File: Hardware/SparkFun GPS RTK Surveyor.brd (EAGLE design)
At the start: 69.1 x 110.1 mm, 189 parts, among them J16 microSD, J17 Qwiic Right Angle, J3 USB Female Type C Connector, J4 Qwiic Right Angle, J5 USB Female Type C Connector, J6 Start Base, J7 Power Switch, Q2 MBT3904DW1T1, U10 MCP73833, U2 3.3V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

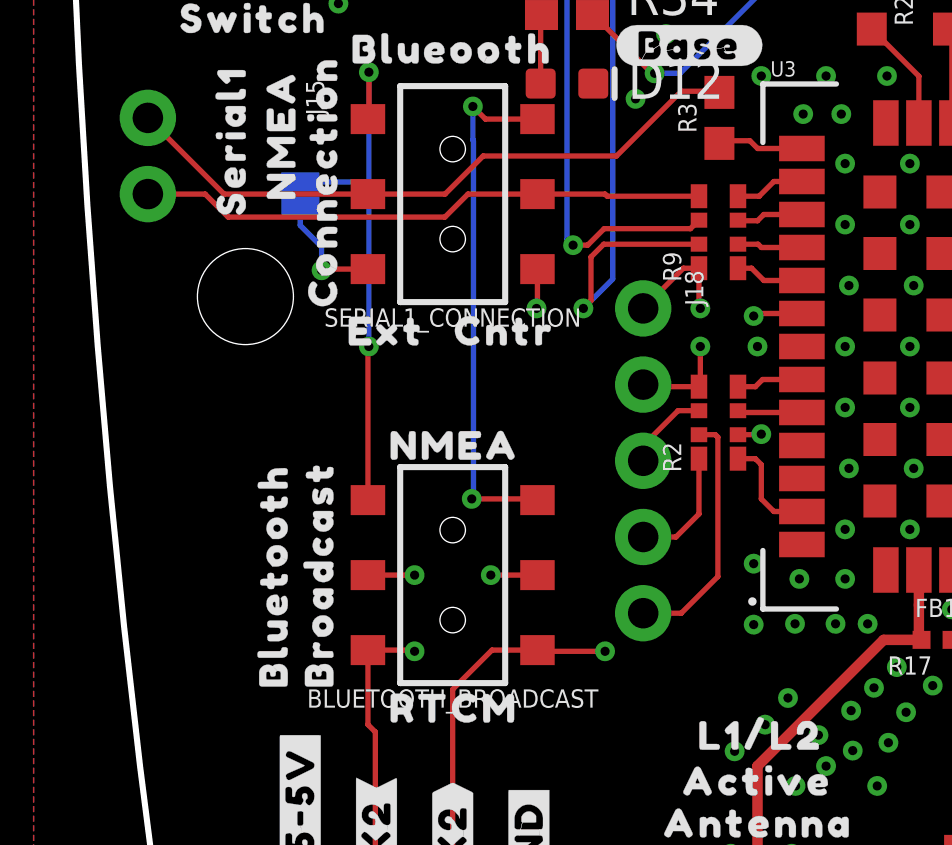
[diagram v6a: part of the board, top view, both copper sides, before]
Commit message: Add slide switch to optionally route PPS to Data port
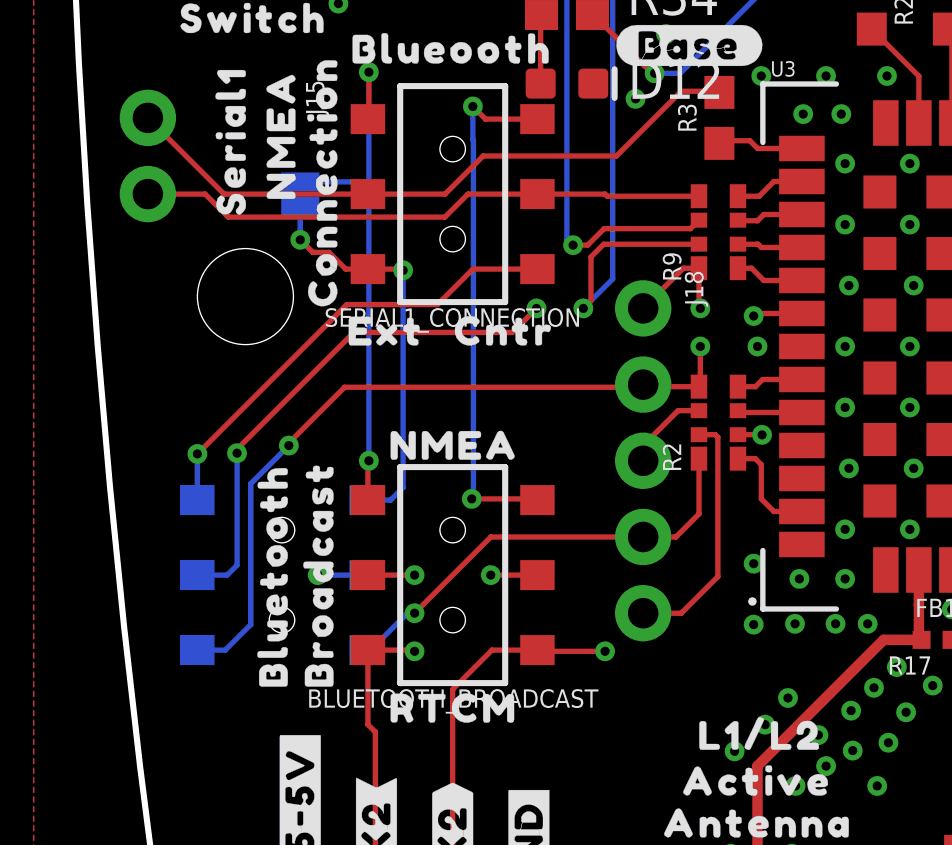
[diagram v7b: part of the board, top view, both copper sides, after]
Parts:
- added U$89: (no value), output:DATA2
- added U$90: (no value), output:PORT3
- added U$91: (no value), output:PPS#RESET0
- added U$92: (no value), output:NMEA#SERIAL1
- added ZED_CONTROL: (no value), SparkFun-Switches:SWITCH_DPDT_SMD_AYZ0202
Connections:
- new net EXTERNAL_SERIAL1_RXI/ZED_!RESET!: J12.2, J2.3, ZED_CONTROL.5
- new net EXTERNAL_SERIAL1_TXO/PPS: J12.3, J2.2, ZED_CONTROL.2
- net ESP_27/ZED_!RESET!: now also ZED_CONTROL.4
- net EXTERNAL_SERIAL1_RXI: now also ZED_CONTROL.6; no longer J12.2, J2.3
- net EXTERNAL_SERIAL1_TXO: now also ZED_CONTROL.3; no longer J12.3, J2.2
- net ZED_PPS_STAT: now also ZED_CONTROL.1
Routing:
- net EXTERNAL_SERIAL1_TXO/PPS: track 0.00 -> 101.6 mm, vias 0 -> 2
- net EXTERNAL_SERIAL1_RXI/ZED_!RESET!: track 0.00 -> 99.7 mm, vias 0 -> 3
- net EXTERNAL_SERIAL1_TXO: track 93.7 -> 13.6 mm
- net EXTERNAL_SERIAL1_RXI: track 83.7 -> 15.4 mm, vias 2 -> 1
- net ESP_27/ZED_!RESET!: track 81.3 -> 102.6 mm, vias 3 -> 4
- net ZED_PPS_STAT: track 55.8 -> 66.6 mm, vias 3 -> 4

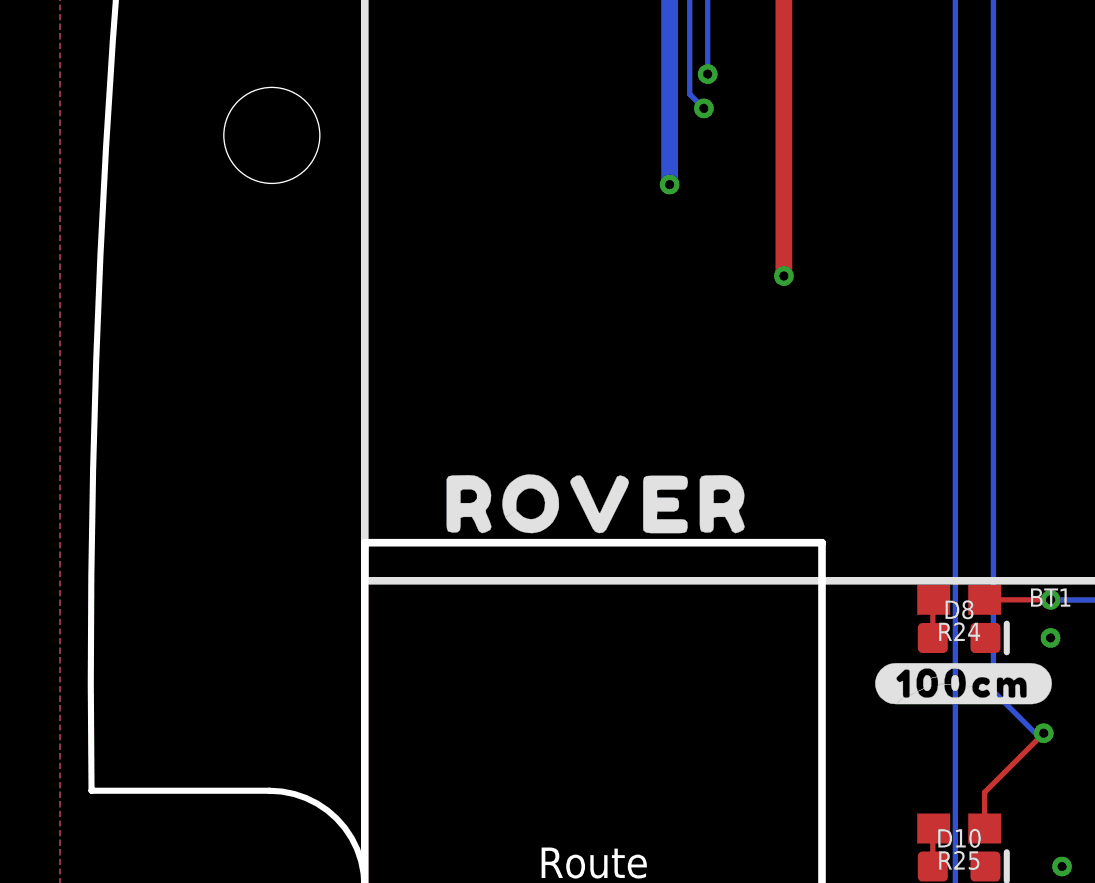
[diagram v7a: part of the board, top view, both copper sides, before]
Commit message: Add internal Qwiic connector
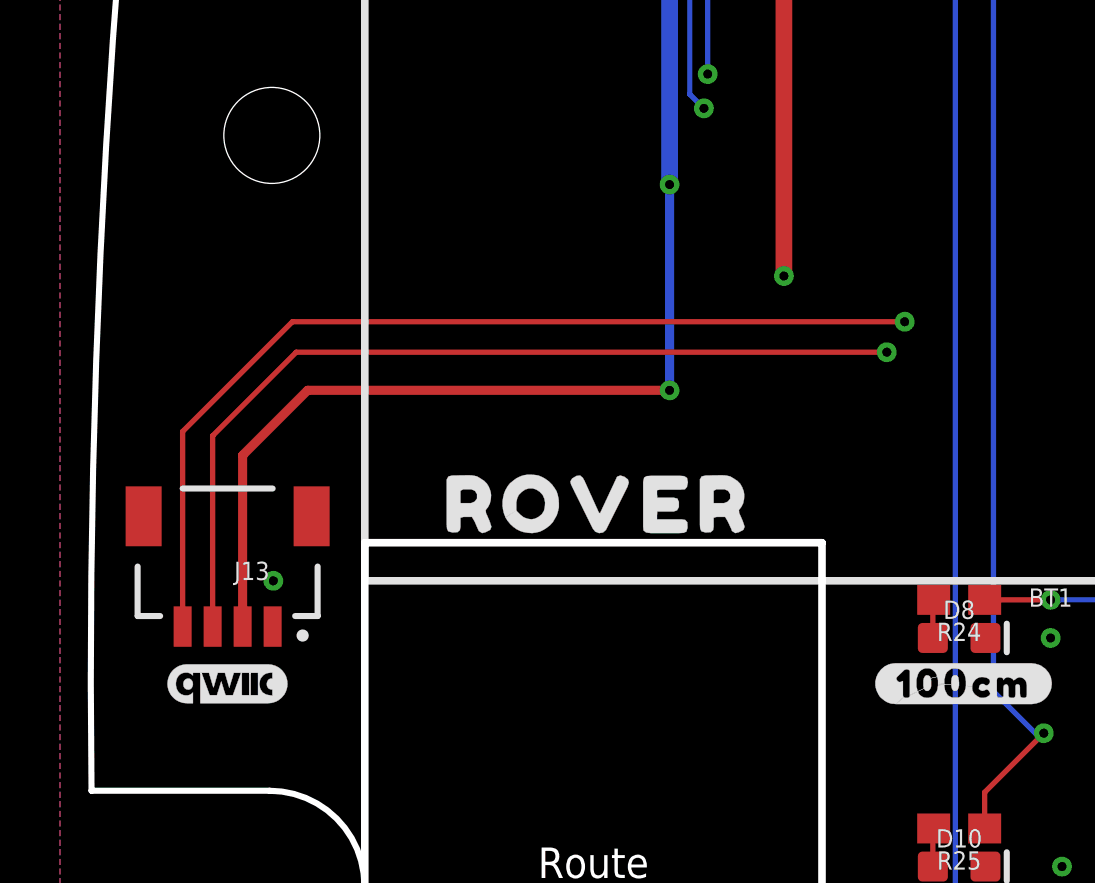
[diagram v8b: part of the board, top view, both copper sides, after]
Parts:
- added J13: Internal, SparkFun-Connectors:JST04_1MM_RA
- added U$93: (no value), SparkFun-Aesthetics:QWIIC_4MM
- J4: value Qwiic Right Angle -> External
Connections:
- net 3.3V: now also J13.2
- net ESP_21/SDA: now also J13.3
- net ESP_22/SCL: now also J13.4
- net GND: now also J13.1
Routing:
- net ESP_22/SCL: track 171.3 -> 203.8 mm, vias 7 -> 8
- net ESP_21/SDA: track 169.6 -> 199.8 mm, vias 7 -> 8
- net 3.3V: track 269.6 -> 297.3 mm, vias 7 -> 8
- net GND: vias 193 -> 194
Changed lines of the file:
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@@
 <layers>
 <layer number="1" name="Top" color="4" fill="1" visible="yes" active="yes"/>
-<layer number="2" name="Horz/GND" color="1" fill="3" visible="yes" active="yes"/>
-<layer number="15" name="Vert" color="4" fill="6" visible="yes" active="yes"/>
+<layer number="2" name="Horz/GND" color="1" fill="3" visible="no" active="yes"/>
+<layer number="15" name="Vert" color="4" fill="6" visible="no" active="yes"/>
 <layer number="16" name="Bottom" color="1" fill="1" visible="yes" active="yes"/>
 <layer number="17" name="Pads" color="2" fill="1" visible="yes" active="yes"/>
@@
 <layer number="19" name="Unrouted" color="6" fill="1" visible="yes" active="yes"/>
 <layer number="20" name="Dimension" color="24" fill="1" visible="yes" active="yes"/>
-<layer number="21" name="tPlace" color="16" fill="1" visible="no" active="yes"/>
+<layer number="21" name="tPlace" color="16" fill="1" visible="yes" active="yes"/>
 <layer number="22" name="bPlace" color="14" fill="1" visible="yes" active="yes"/>
 <layer number="23" name="tOrigins" color="15" fill="1" visible="yes" active="yes"/>
@@
 <element name="JP21" library="SparkFun-Aesthetics" package="FIDUCIAL-MICRO" value="FIDUCIALUFIDUCIAL" x="54.61" y="4.35" smashed="yes"/>
 <element name="JP61" library="SparkFun-Aesthetics" package="FIDUCIAL-MICRO" value="FIDUCIALUFIDUCIAL" x="-3.63" y="105.23" smashed="yes"/>
-<element name="J4" library="SparkFun-Connectors" package="JST04_1MM_RA" value="Qwiic Right Angle" x="25.4" y="4.81" smashed="yes" rot="MR0">
+<element name="J4" library="SparkFun-Connectors" package="JST04_1MM_RA" value="External" x="25.4" y="4.81" smashed="yes" rot="MR0">
 <attribute name="NAME" x="26.797" y="2.651" size="0.6096" layer="26" font="vector" ratio="20" rot="MR0"/>
 <attribute name="PROD_ID" value="CONN-13694" x="25.4" y="4.81" size="1.778" layer="28" rot="MR0" display="off"/>
@@
 <element name="U$91" library="output" package="PPS#RESET0" value="" x="-1.905" y="14.478" smashed="yes" rot="MR0"/>
 <element name="U$92" library="output" package="NMEA#SERIAL1" value="" x="-2.032" y="23.749" smashed="yes" rot="MR0"/>
+<element name="J13" library="SparkFun-Connectors" package="JST04_1MM_RA" value="Internal" x="-4.572" y="61.976" smashed="yes" rot="R180">
+<attribute name="NAME" x="-3.175" y="64.135" size="0.6096" layer="25" font="vector" ratio="20" rot="R180"/>
+<attribute name="PROD_ID" value="CONN-13694" x="-4.572" y="61.976" size="1.778" layer="27" font="vector" ratio="15" rot="R180" display="off"/>
+<attribute name="VALUE" x="-2.921" y="65.278" size="0.6096" layer="27" font="vector" ratio="20" rot="R180"/>
+</element>
+<element name="U$93" library="SparkFun-Aesthetics" package="QWIIC_4MM" value="" x="-4.572" y="60.055" smashed="yes"/>
 </elements>
 <signals>
@@
 <via x="26.2175" y="3.2305" extent="1-16" drill="0.3048"/>
 <wire x1="26.67" y1="11.43" x2="26.67" y2="3.683" width="0.5588" layer="2"/>
+<contactref element="J13" pad="2"/>
+<wire x1="-4.072" y1="61.976" x2="-4.072" y2="67.683" width="0.3048" layer="1"/>
+<wire x1="-1.905" y1="69.85" x2="10.16" y2="69.85" width="0.3048" layer="1"/>
+<wire x1="-4.072" y1="67.683" x2="-1.905" y2="69.85" width="0.3048" layer="1"/>
+<via x="10.16" y="69.85" extent="1-16" drill="0.3048"/>
+<wire x1="10.16" y1="69.85" x2="10.16" y2="76.708" width="0.3048" layer="16"/>
 </signal>
 <signal name="GND">
@@
 <contactref element="J17" pad="1"/>
 <via x="36.83" y="12.573" extent="1-16" drill="0.3048"/>
+<contactref element="J13" pad="1"/>
+<via x="-3.048" y="63.5" extent="1-16" drill="0.3048"/>
 </signal>
 <signal name="ESP_22/SCL">
@@
 <wire x1="15.414" y1="99.14" x2="15.367" y2="99.187" width="0.254" layer="16"/>
 <via x="15.367" y="99.187" extent="1-16" drill="0.3048"/>
-<wire x1="15.367" y1="99.187" x2="17.526" y2="97.028" width="0.1778" layer="15"/>
-<wire x1="17.526" y1="97.028" x2="17.526" y2="42.7093" width="0.1778" layer="15"/>
+<wire x1="15.367" y1="99.187" x2="17.4625" y2="97.0915" width="0.1778" layer="15"/>
 <via x="16.002" y="38.862" extent="1-16" drill="0.3048"/>
 <wire x1="16.002" y1="38.862" x2="16.002" y2="39.9415" width="0.1778" layer="2"/>
@@
 <wire x1="18.8849" y1="40.90075" x2="18.24315" y2="40.259" width="0.1778" layer="15"/>
 <wire x1="18.8849" y1="41.3504" x2="18.8849" y2="40.90075" width="0.1778" layer="15"/>
-<wire x1="17.526" y1="42.7093" x2="18.8849" y2="41.3504" width="0.1778" layer="15"/>
+<wire x1="18.8849" y1="41.3504" x2="17.526" y2="42.7093" width="0.1778" layer="15"/>
 <contactref element="U7" pad="7"/>
 <wire x1="23.9" y1="4.81" x2="23.9" y2="9.152" width="0.1778" layer="16"/>
@@
 <wire x1="35.56" y1="12.684" x2="34.29" y2="13.954" width="0.1778" layer="1"/>
 <wire x1="34.29" y1="13.954" x2="34.29" y2="13.97" width="0.1778" layer="1"/>
+<contactref element="J13" pad="4"/>
+<wire x1="-6.072" y1="61.976" x2="-6.072" y2="68.477" width="0.1778" layer="1"/>
+<wire x1="-6.072" y1="68.477" x2="-2.413" y2="72.136" width="0.1778" layer="1"/>
+<wire x1="17.526" y1="42.7093" x2="17.526" y2="70.40285" width="0.1778" layer="15"/>
+<wire x1="17.526" y1="70.40285" x2="17.9959" y2="70.87275" width="0.1778" layer="15"/>
+<wire x1="17.9959" y1="70.87275" x2="17.9959" y2="72.136" width="0.1778" layer="15"/>
+<via x="17.9959" y="72.136" extent="1-16" drill="0.3048"/>
+<wire x1="-2.413" y1="72.136" x2="17.9959" y2="72.136" width="0.1778" layer="1"/>
+<wire x1="17.9959" y1="72.136" x2="17.4752" y2="72.6567" width="0.1778" layer="15"/>
+<wire x1="17.4752" y1="97.0788" x2="17.4625" y2="97.0915" width="0.1778" layer="15"/>
+<wire x1="17.4752" y1="72.6567" x2="17.4752" y2="97.0788" width="0.1778" layer="15"/>
 </signal>
 <signal name="ESP_21/SDA">
@@
 <wire x1="17.162" y1="95.33" x2="15.574" y2="95.33" width="0.1778" layer="16"/>
 <wire x1="15.574" y1="95.33" x2="15.494" y2="95.25" width="0.1778" layer="16"/>
-<wire x1="17.1196" y1="93.6244" x2="17.1196" y2="42.2318" width="0.1778" layer="15"/>
+<wire x1="17.1196" y1="93.6244" x2="17.1196" y2="71.12" width="0.1778" layer="15"/>
+<wire x1="17.1196" y1="71.12" x2="17.1196" y2="42.2318" width="0.1778" layer="15"/>
 <wire x1="15.494" y1="95.25" x2="17.1196" y2="93.6244" width="0.1778" layer="15"/>
 <via x="18.034" y="40.894" extent="1-16" drill="0.3048"/>
@@
 <wire x1="32.528" y1="11.922" x2="31.75" y2="12.7" width="0.1778" layer="1"/>
 <wire x1="31.75" y1="12.7" x2="31.75" y2="13.97" width="0.1778" layer="1"/>
+<contactref element="J13" pad="3"/>
+<wire x1="-5.072" y1="61.976" x2="-5.072" y2="68.334" width="0.1778" layer="1"/>
+<wire x1="-5.072" y1="68.334" x2="-2.286" y2="71.12" width="0.1778" layer="1"/>
+<wire x1="-2.286" y1="71.12" x2="17.399" y2="71.12" width="0.1778" layer="1"/>
+<via x="17.399" y="71.12" extent="1-16" drill="0.3048"/>
+<wire x1="17.399" y1="71.12" x2="17.1196" y2="71.12" width="0.1778" layer="15"/>
 </signal>
 <signal name="TXLV">
